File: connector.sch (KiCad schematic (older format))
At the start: 15 parts

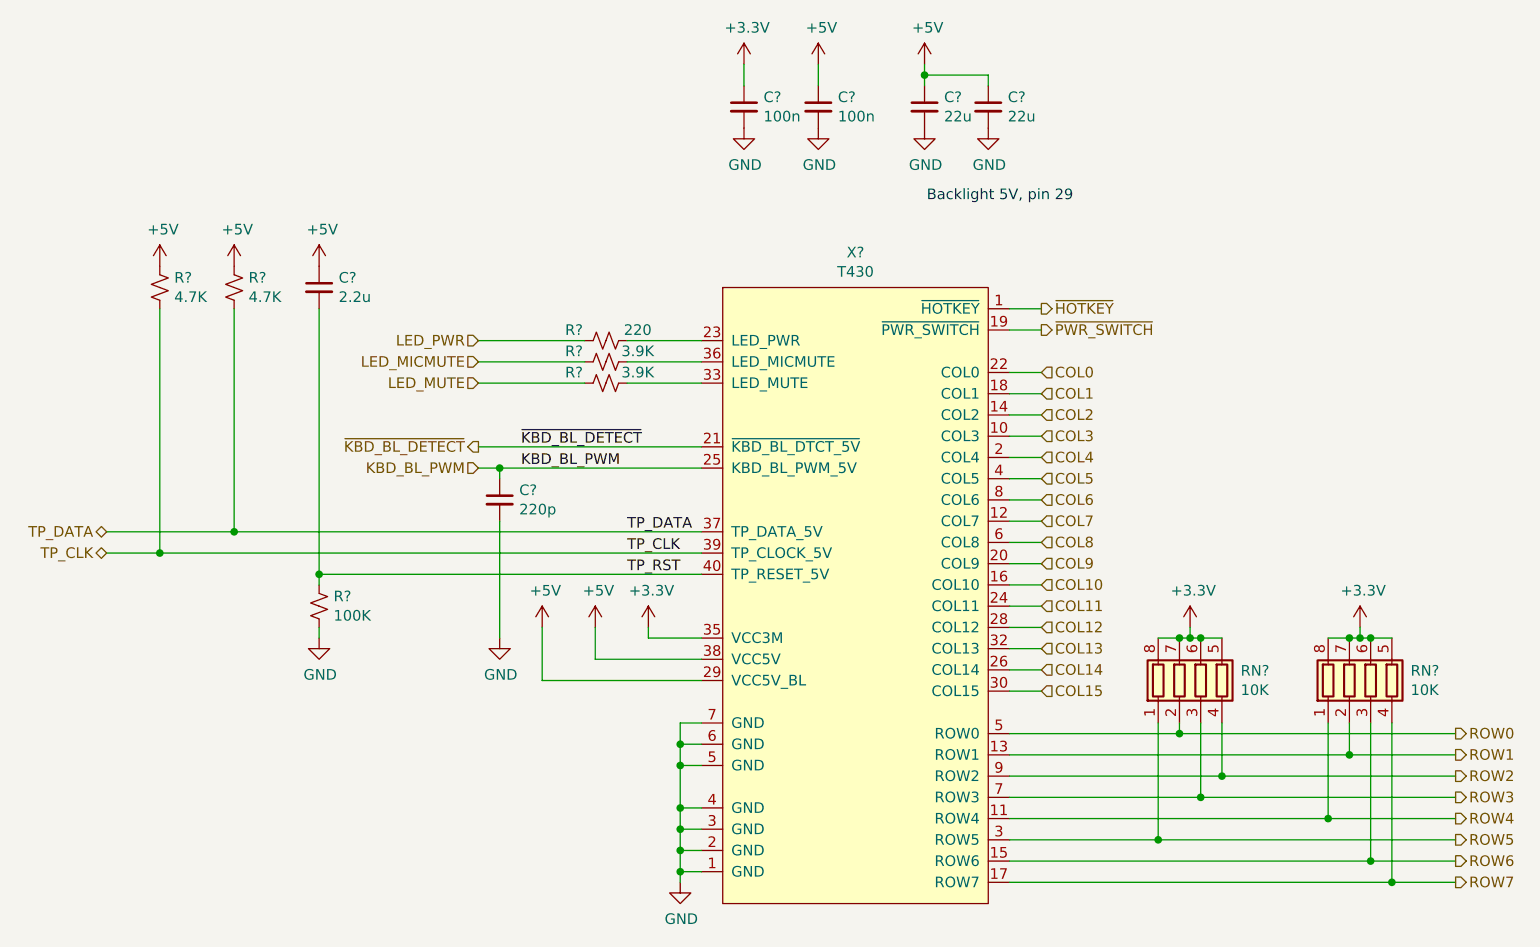
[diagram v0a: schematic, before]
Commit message: Updated footprints and started PCB
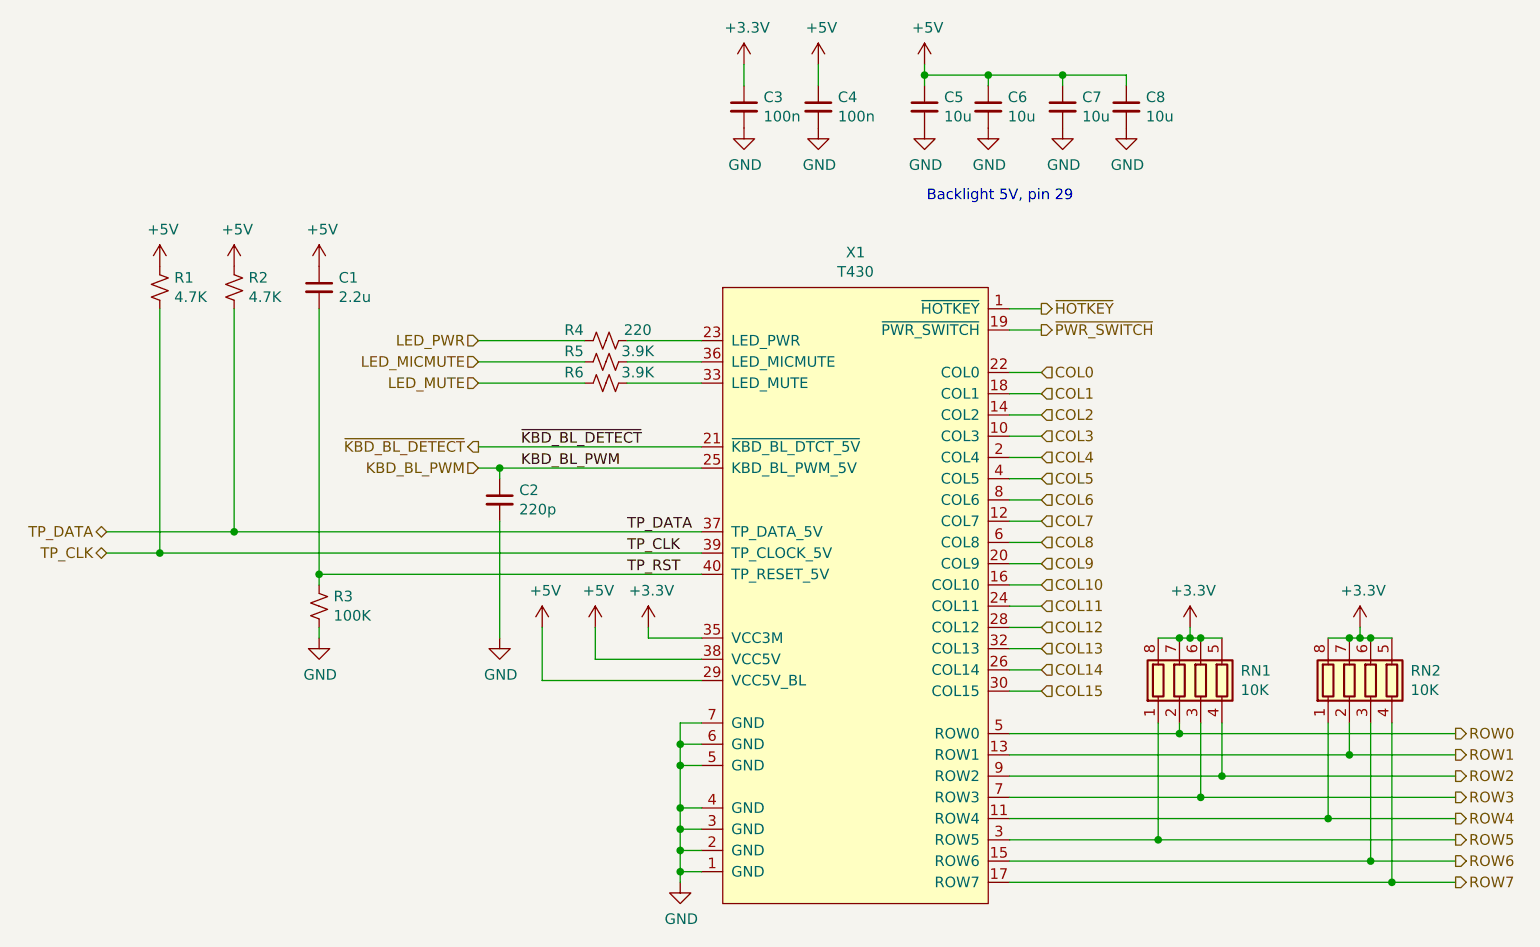
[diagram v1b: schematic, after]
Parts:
- added C7, C8: 10u, Capacitor_SMD:C_0805_2012Metric_Pad1.15x1.40mm_HandSolder, symbol Device:C_Small
- C1: renamed from C?; footprint (none) -> Capacitor_SMD:C_0805_2012Metric_Pad1.15x1.40mm_HandSolder
- C2, C3, C4: renamed from C?; footprint (none) -> Capacitor_SMD:C_0603_1608Metric
- C5, C6: renamed from C?; value 22u -> 10u; footprint (none) -> Capacitor_SMD:C_0805_2012Metric_Pad1.15x1.40mm_HandSolder
- R1, R2, R3, R4, R5, R6: renamed from R?; footprint (none) -> Resistor_SMD:R_0603_1608Metric_Pad1.05x0.95mm_HandSolder
- RN1, RN2: renamed from RN?; footprint (none) -> Resistor_SMD:R_Array_Concave_4x0603
- X1: renamed from X?; footprint (none) -> thinkpad_kbd_connectors:AA01B-S040VA1-R3000
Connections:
- net +5V: now also C7.1, C8.1
- net GND: now also C7.2, C8.2
